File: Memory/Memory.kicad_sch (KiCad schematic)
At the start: 13 parts, among them J1 Buss, U1 FM1808, U2 FM1608, U3 FM1608, U4 28C64, U5 74LS139

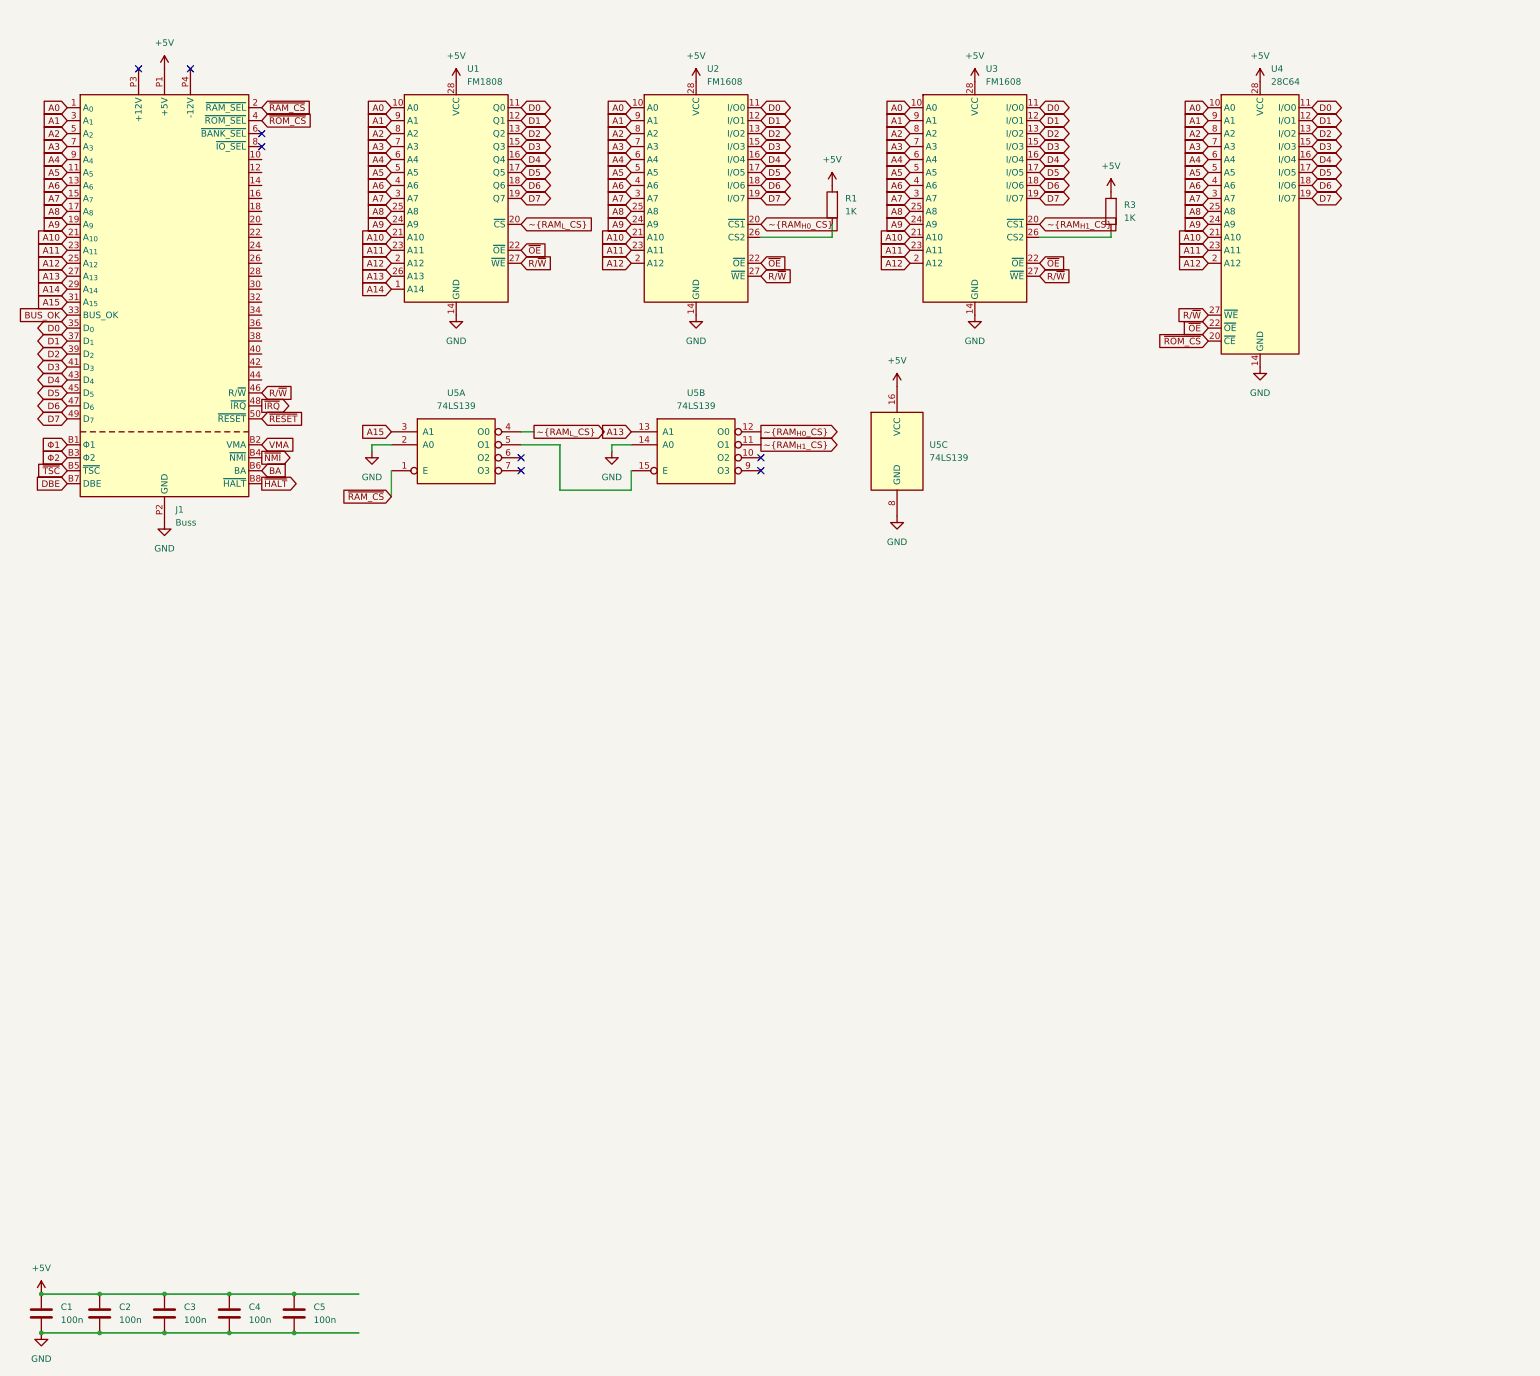
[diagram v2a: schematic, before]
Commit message: ordered memory board
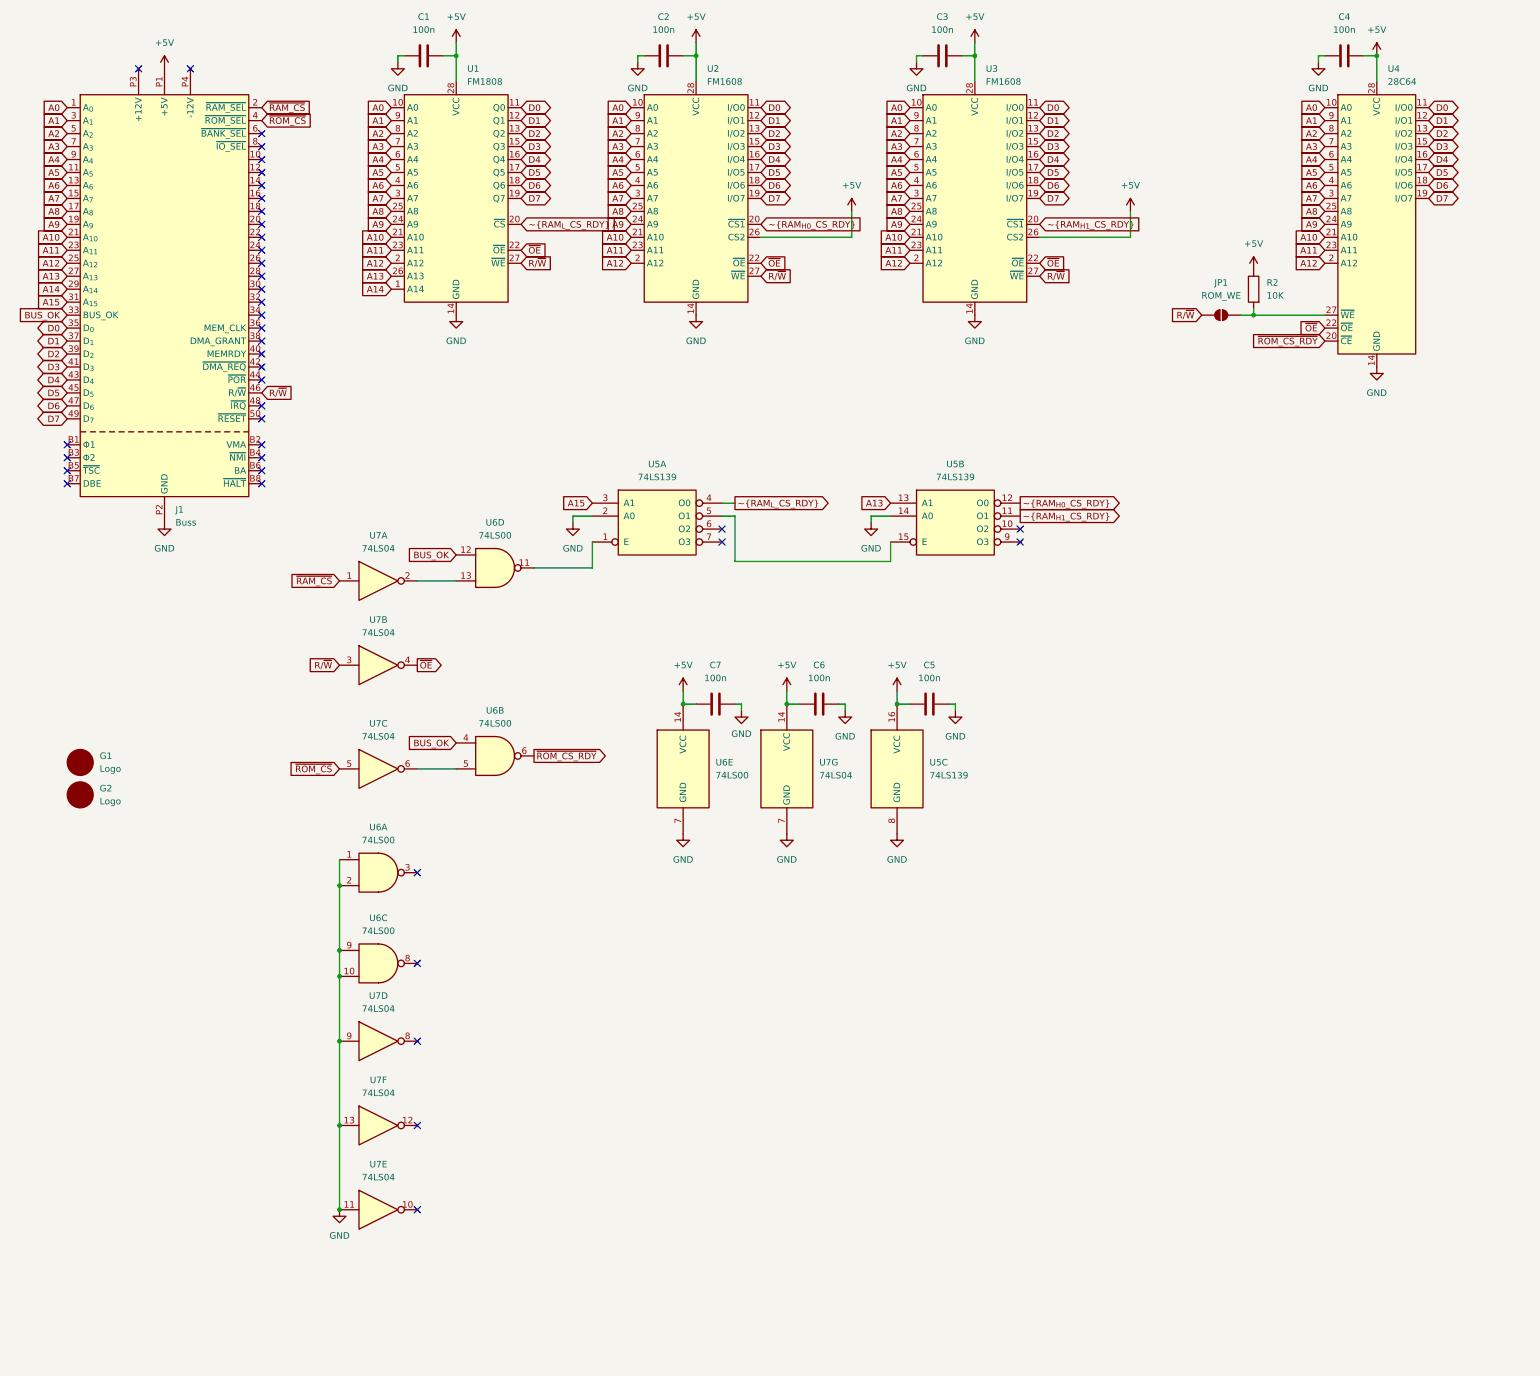
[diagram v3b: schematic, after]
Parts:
- removed R1, R3: 1K, Resistor_THT:R_Axial_DIN0207_L6.3mm_D2.5mm_P7.62mm_Horizontal, symbol Device:R
- added C6, C7: 100n, 0-Footprints:C_Disc_D5.0mm_W2.5mm_P5.00mm, symbol Device:C
- added G1: Logo, 0-Footprints:Crank, symbol 0-Symbols:Logo
- added G2: Logo, 0-Footprints:crankery_small, symbol 0-Symbols:Logo
- added JP1: ROM_WE, 0-Footprints:SolderJumper-2_P1.3mm_Open_RoundedPad1.0x1.5mm, symbol Jumper:SolderJumper_2_Open
- added R2: 10K, 0-Footprints:R_Axial_DIN0204_L3.6mm_D1.6mm_P7.62mm_Horizontal, symbol Device:R
- added U6: 74LS00, 0-Footprints:DIP-14_W7.62mm, symbol 74xx:74LS00
- added U7: 74LS04, 0-Footprints:DIP-14_W7.62mm, symbol 74xx:74LS04
- C1, C2, C3, C4, C5: footprint Capacitor_THT:C_Disc_D3.0mm_W1.6mm_P2.50mm -> 0-Footprints:C_Disc_D5.0mm_W2.5mm_P5.00mm
- J1: footprint (none) -> 0-Footprints:Card
- U4: footprint Package_DIP:DIP-28_W15.24mm -> 0-Footprints:DIP-28_W15.24mm
- U5: footprint Package_DIP:DIP-16_W7.62mm -> 0-Footprints:DIP-16_W7.62mm
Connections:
- net +5V: now also C1.1, C2.1, C3.1, C4.1, U2.26 (CS2), U3.26 (CS2), C6.2, C7.2, R2.1, U6.14 (VCC), U7.14 (VCC); no longer C1.2, C2.2, C3.2, C4.2
- net BUS_OK: now also U6.12, U6.4
- net GND: now also C1.2, C2.2, C3.2, C4.2, C6.1, C7.1, U6.1, U6.10, U6.2, U6.7 (GND), U6.9, U7.11, U7.13, U7.7 (GND), U7.9; no longer C1.1, C2.1, C3.1, C4.1
- net R/~{W}: now also JP1.1 (A), U7.3; no longer U4.27 (~{WE})
- net ~{OE}: now also U7.4
- net ~{RAM_CS}: now also U7.1; no longer U5.1 (E)
- net ~{ROM_CS}: now also U7.5; no longer U4.20 (~{CE})
- net BA: no longer names the net of J1.B6 (BA)
- net DBE: no longer names the net of J1.B7 (DBE)
- net VMA: no longer names the net of J1.B2 (VMA)
- net ~{HALT}: no longer names the net of J1.B8 (~{HALT})
- net ~{IRQ}: no longer names the net of J1.48 (~{IRQ})
- net ~{NMI}: no longer names the net of J1.B4 (~{NMI})
- net ~{RAM_{H0}_CS} renamed ~{RAM_{H0}_CS_RDY}
- net ~{RAM_{H1}_CS} renamed ~{RAM_{H1}_CS_RDY}
- net ~{RAM_{L}_CS} renamed ~{RAM_{L}_CS_RDY}
- net ~{RESET}: no longer names the net of J1.50 (~{RESET})
- net ~{TSC}: no longer names the net of J1.B5 (~{TSC})
- net Φ1: no longer names the net of J1.B1 (Φ1)
- net Φ2: no longer names the net of J1.B3 (Φ2)
- new net: U5.1 (E), U6.11
- new net: U6.13, U7.2
- new net: JP1.2 (B), R2.2, U4.27 (~{WE})
- new net: U6.5, U7.6
- new net ~{ROM_CS_RDY}: U4.20 (~{CE}), U6.6
- no-connect marks 8 -> 41
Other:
- moved on the sheet: C1, C2, C3, C4, C5, U4, U5A, U5B, U5C

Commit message: commit-a-palooza after refactoring out the singleton on Machine, and upgrading to kicad 10
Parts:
- added unit 2 of U6
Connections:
- net BUS_OK: now also U6.4; no longer U6.4
- net ~{ROM_CS_RDY}: now also U6.6; no longer U6.6
- net at U7.6: now also U6.5; no longer U6.5
